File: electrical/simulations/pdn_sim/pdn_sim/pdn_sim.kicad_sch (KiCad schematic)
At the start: 7 parts

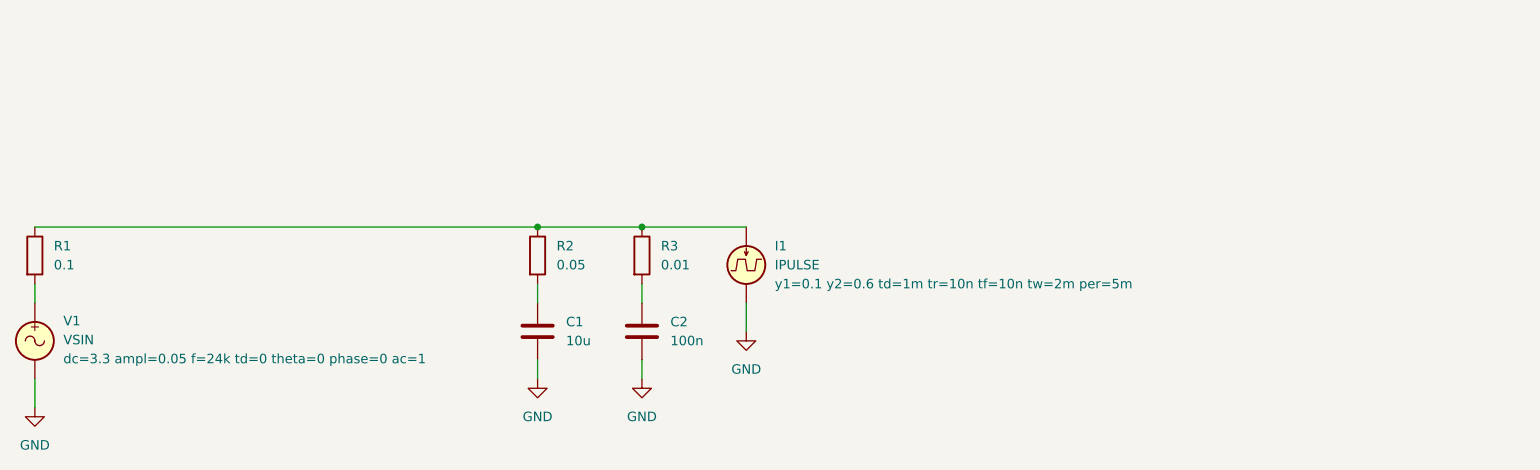
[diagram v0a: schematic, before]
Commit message: PDN sim fixes and additions
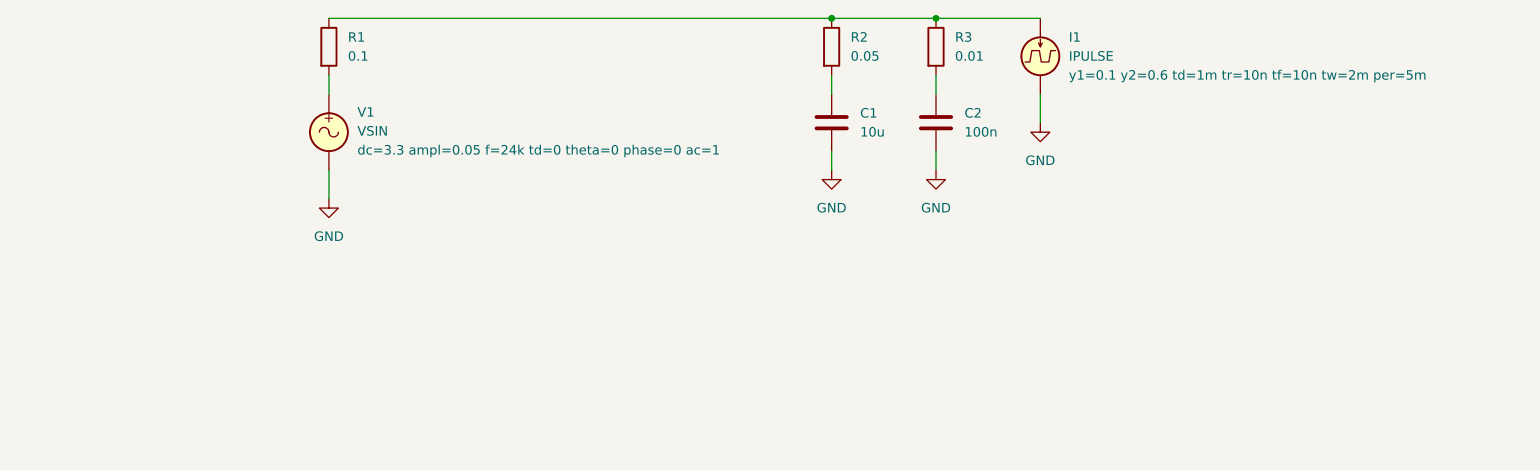
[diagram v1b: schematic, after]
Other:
- moved on the sheet: C1, C2, I1, R1, R2, R3, V1
